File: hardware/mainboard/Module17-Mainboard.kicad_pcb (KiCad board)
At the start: 4 copper layers, 100 x 83.3 mm, 206 parts, among them IC301 LM4991MA, J301 CAT_TX, J302 CAT_RX, J401 Radio, J402 USB_C, J403 Radio_Opt, J404 Kenwood-3.5, J405 Kenwood-2.5, J406 2.54mm Header 7p, J407 KH-RJ45-58-8P8C, J408 STLink, J409 UART, J410 Speaker, J411 +12V, J412 Hirose FH12-26S-0.5SH(55), J413 Molex 532610271, Q201 MMBT3904, Q202 IRLML2244, Q301 IRLML2060, Q302 BSS138, Q303 BSS138, SW201 Tactile switch, SW202 Tactile switch, SW203 Tactile switch, SW204 Tactile switch, SW205 Tactile switch, SW206 Tactile switch, SW207 Tactile switch, SW208 Tactile switch, U201 STM32F405RGTx, U202 TPS7A2033, U203 TP6841S6, U301 MCP6002, U302 MAX9814, U401 USBLC6-2SC6, U501 MCP4551-103, U502 MCP4551-103, U503 MCP6002, U504 MCP6002, Y201 8 MHz

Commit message: Mainboard Rev 0.99b
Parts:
- removed the REF** at (250.6, 112.5)
- removed the REF** at (233.8, 57.5)
- added C317: 100n, Capacitor_SMD:C_0603_1608Metric, F.Cu at (175.2, 114.0)
- added R233: 0, Resistor_SMD:R_0603_1608Metric, F.Cu at (186.3, 86.2)
- added R320: 430, Resistor_SMD:R_0603_1608Metric, F.Cu at (176.0, 111.6)
- added REF**: M17_Module17_QR_Code, Module17:M17_Module17_QR_Code, B.Cu at (255.0, 88.5)
- J401: footprint Connector_Dsub:DSUB-9_Female_Horizontal_P2.77x2.84mm_EdgePinOffset4.94mm_Housed_MountingHolesOffset7.48mm -> Connector_Dsub:DSUB-9_Female_Horizontal_P2.77x2.84mm_EdgePinOffset7.70mm_Housed_MountingHolesOffset9.12mm
- moved JP201 2.41 mm to (189.2, 87.5), turned to 180 degrees
- moved J402 0.15 mm to (217.8, 49.3)
- moved RV501 0.15 mm to (245.2, 50.5)
- moved RV502 0.15 mm to (260.7, 50.5)
- moved C209 0.10 mm to (190.8, 80.1)
- moved C211 0.10 mm to (189.2, 80.1)
- moved U504 0.10 mm to (251.9, 56.8)
- turned TP304 to 0 degrees
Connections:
- U302 pad 6: AUDIO_MIC -> Net-(U302-MICOUT)
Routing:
- net Net-(JP201-A): track 5.12 -> 10.5 mm
- net +5V: track 243.3 -> 246.5 mm
- net Net-(U302-MICOUT): track 0.00 -> 2.88 mm
- net GND: track 11.9 -> 14.2 mm, vias 1084 -> 1087
- net AUDIO_MIC: track 17.3 -> 15.6 mm
- net NRST: track 81.5 -> 82.3 mm
- net VDD: track 349.5 -> 350.0 mm
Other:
- board size 100 x 83.3 mm -> 100 x 83 mm
- board text added: "100.0000 mm x 83.0000 mm"
- board text added: "Getting Started"
- board text added: "Revision 0.99b 04.2024"
- board text removed: "100.0000 mm x 83.3000 mm"
- board text removed: "Revision 0.99b 12.2023"

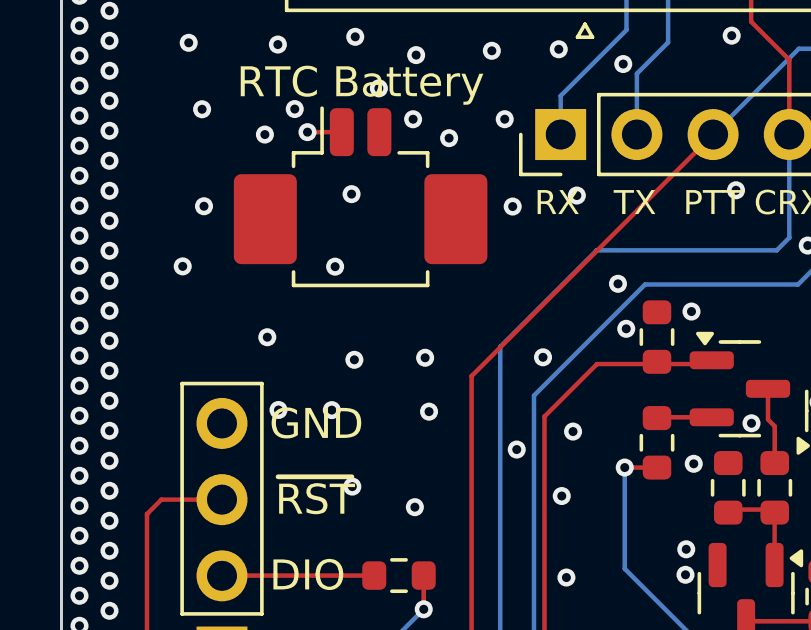
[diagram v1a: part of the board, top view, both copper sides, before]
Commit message: Added polarity on RTC battery connector
Added polarity marking on sikscreen layer.
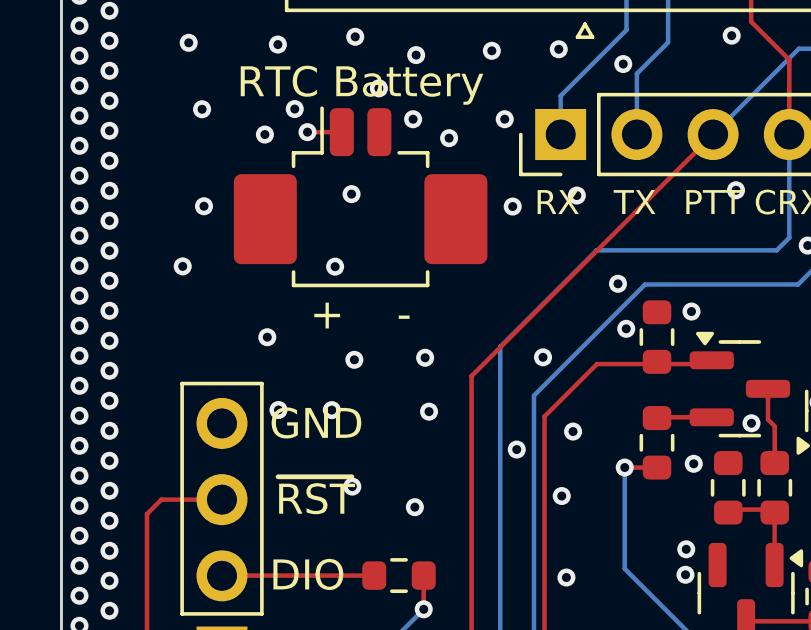
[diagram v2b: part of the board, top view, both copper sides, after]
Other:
- board text added: "+ -"

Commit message: Updated Mainboard PCB to revision 1.0
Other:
- board text added: "ON4MOD, DB9MAT, SP5WWP"
- board text added: "Revision 1.0 06.2024"
- board text removed: "DB9MAT, SP5WWP, ON4MOD"
- board text removed: "Revision 0.99b 04.2024"
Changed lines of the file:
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@@
 	(title_block
 		(title "Module17")
-		(date "2024-04-25")
-		(rev "Rev 0.99b")
-		(company "OpenHT")
+		(date "2024-06-19")
+		(rev "Rev 1.0")
+		(company "M17 Project")
 		(comment 1 "Morgan - ON4MOD")
 		(comment 2 "Mathis - DB9MAT")
@@
 		)
 	)
-	(gr_text "Revision 0.99b\n04.2024"
+	(gr_text "Revision 1.0\n06.2024"
 		(at 251.8 56.775 90)
 		(layer "B.SilkS")
@@
 		)
 	)
-	(gr_text "DB9MAT, SP5WWP,\nON4MOD"
+	(gr_text "ON4MOD, DB9MAT,\nSP5WWP\n"
 		(at 256.74 56.795 90)
 		(layer "B.SilkS")
@@
 			(font
 				(size 1 1)
-				(thickness 0.15)
+				(thickness 0.16)
 			)
 		)
